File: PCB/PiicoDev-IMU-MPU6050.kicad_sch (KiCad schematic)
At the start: 25 parts, among them J1 , J2 , J3 , J4 Address, J5 Address, SW1 SW_DIP_x01, U1 MPU-6050

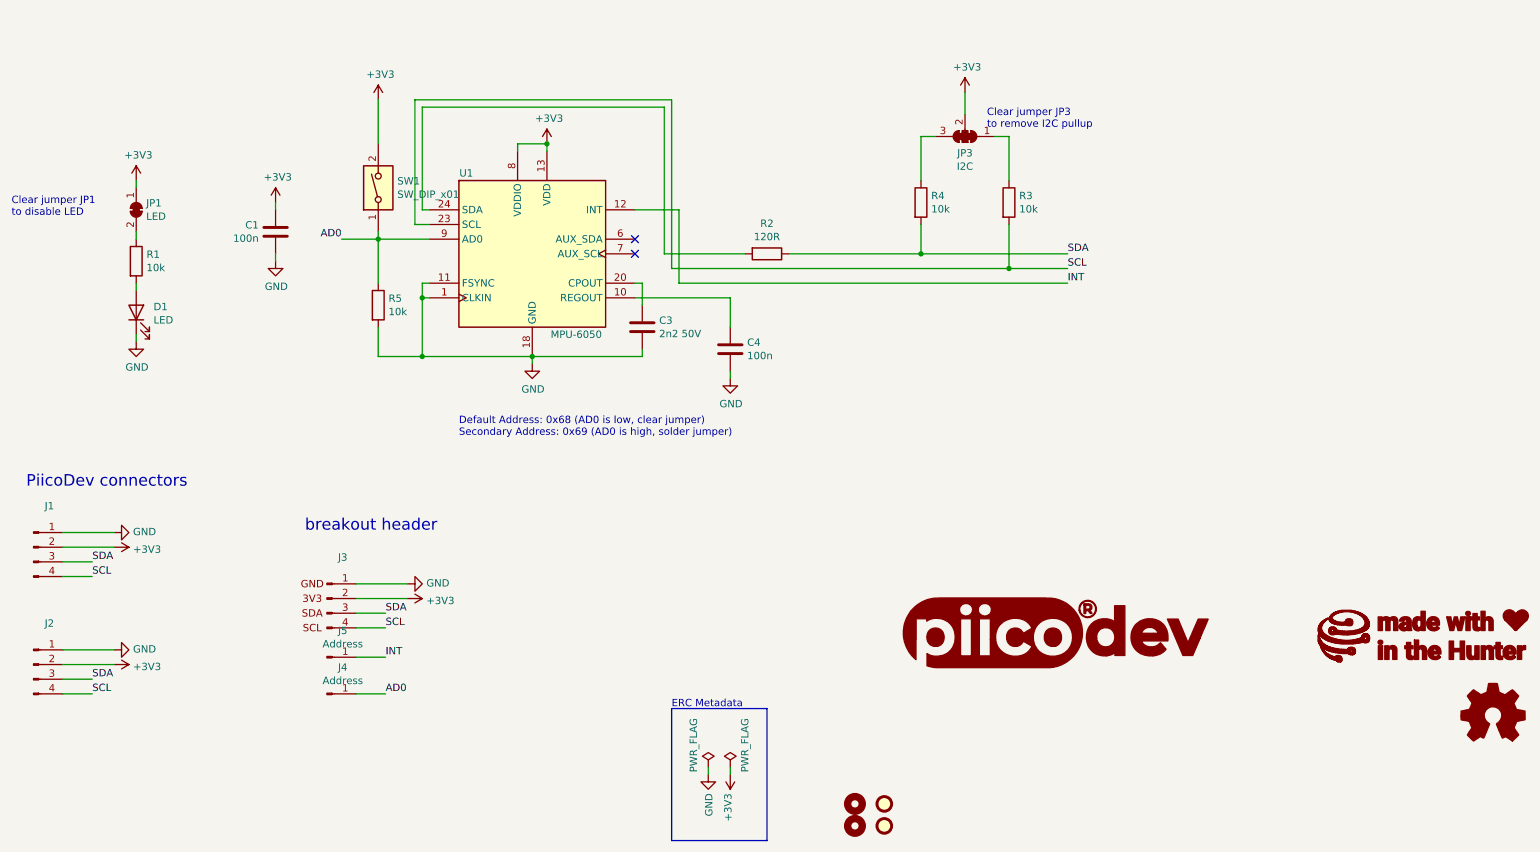
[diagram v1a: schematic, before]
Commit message: Upgrade to v14 and KiCad6
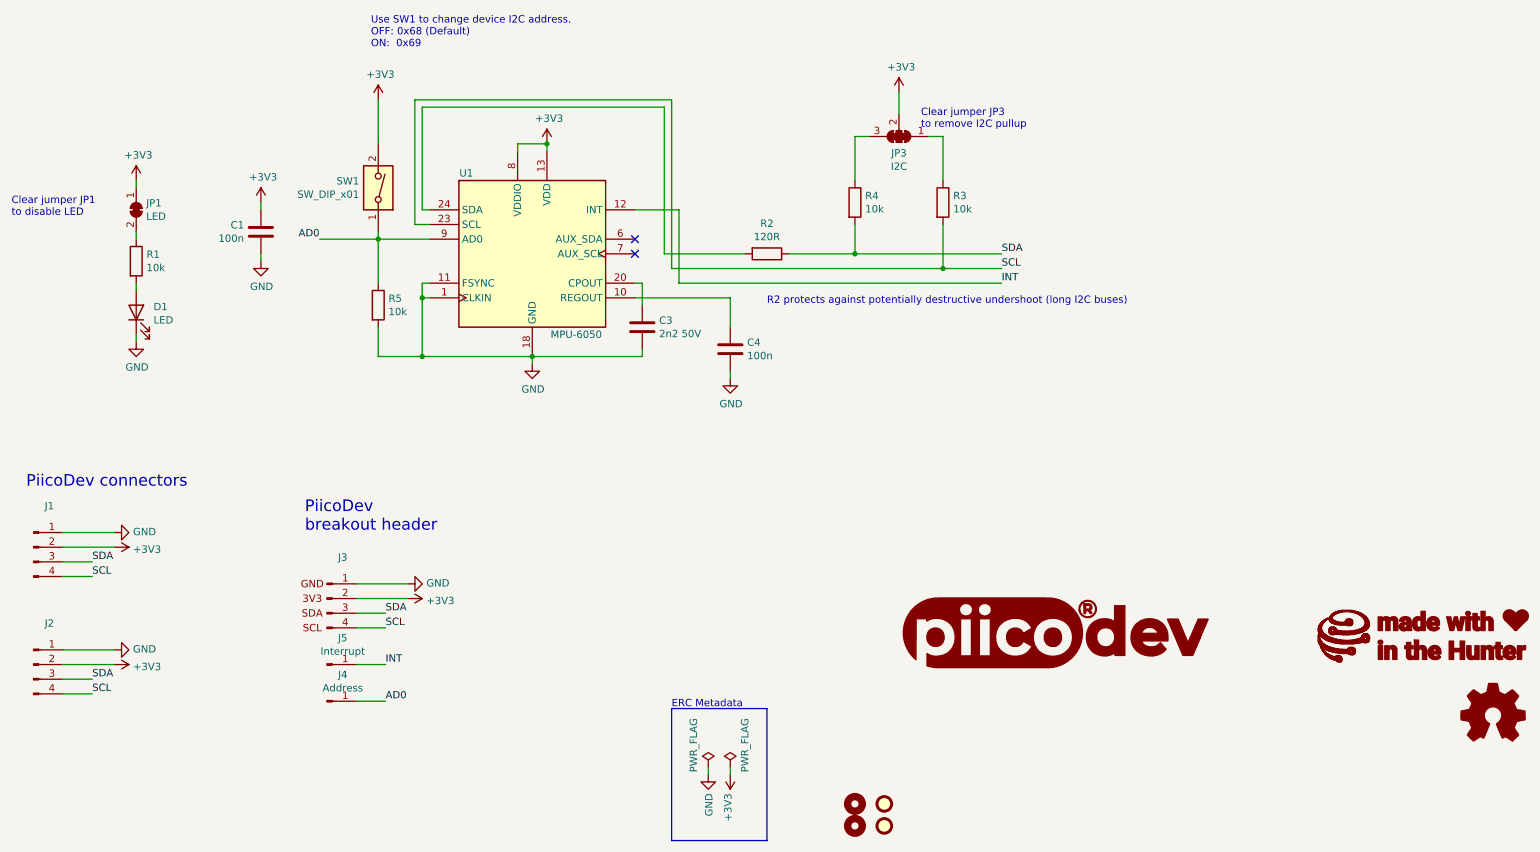
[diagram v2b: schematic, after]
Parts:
- J5: value Address -> Interrupt
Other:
- note added: "PiicoDev breakout header"
- note added: "R2 protects against potentially destructive undershoot (long I2C buses)"
- note added: "Use SW1 to change device I2C address. OFF: 0x68 (Default) ON: 0x69"
- note removed: "Default Address: 0x68 (AD0 is low, clear jumper) Secondary Address: 0x69 (AD0 is high, solder jumper)"
- note removed: "breakout header"
- moved on the sheet: C1, J4, J5, JP3, R3, R4, SW1
